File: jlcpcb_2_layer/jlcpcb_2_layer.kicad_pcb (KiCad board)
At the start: 2 copper layers, 2 parts

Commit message: updated JLCPCB 2layer template with new date
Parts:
- N2: value V20171120 -> V20180719
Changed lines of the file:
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@@
     (links 0)
     (no_connects 0)
-    (area 143.609505 97.866906 152.473829 108.0274)
+    (area 0 0 0 0)
     (thickness 1.6)
     (drawings 0)
@@
       (effects (font (size 1 1) (thickness 0.15)))
     )
-    (fp_text value V20171120 (at 0 0) (layer F.SilkS)
-      (effects (font (size 1 1) (thickness 0.15)))
-    )
+    (fp_text value V20180719 (at 0 0) (layer F.SilkS)
+      (effects (font (size 1 1) (thickness 0.15)))
+    )

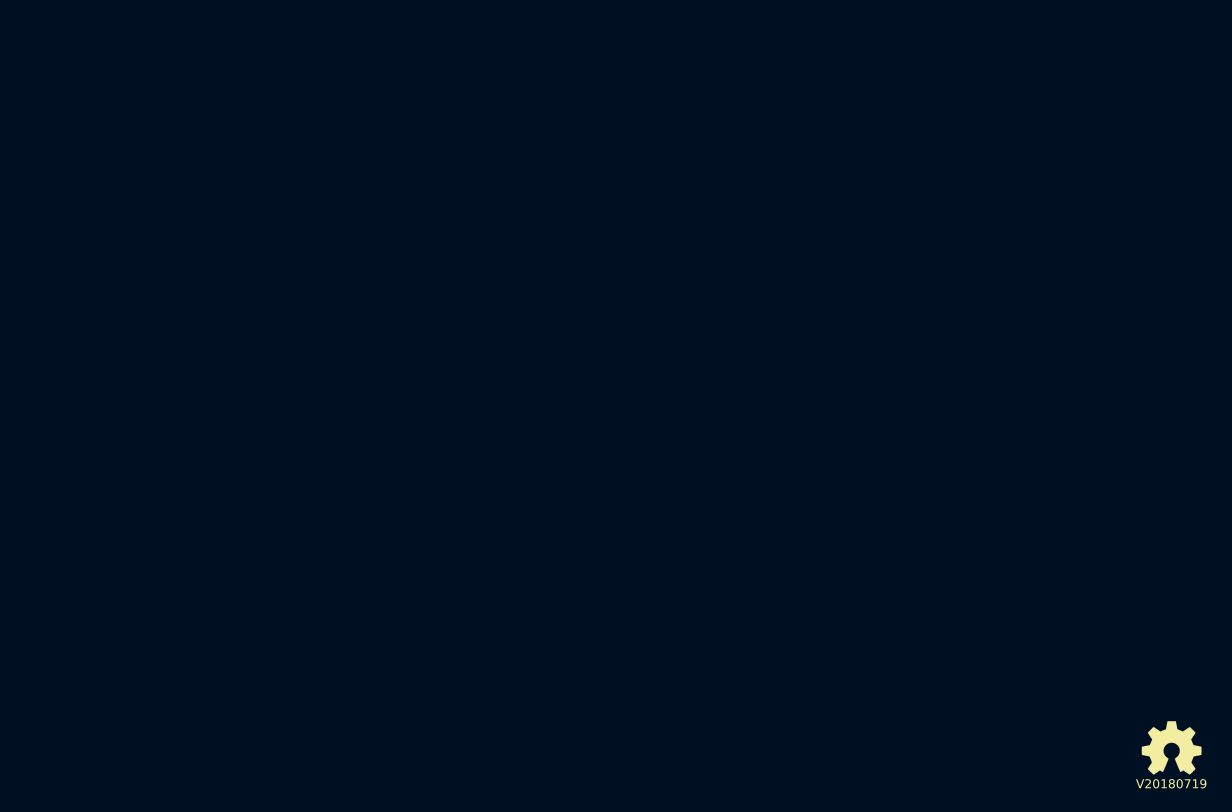
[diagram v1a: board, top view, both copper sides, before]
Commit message: updated jlcpcb 2 layer template to kicad 6
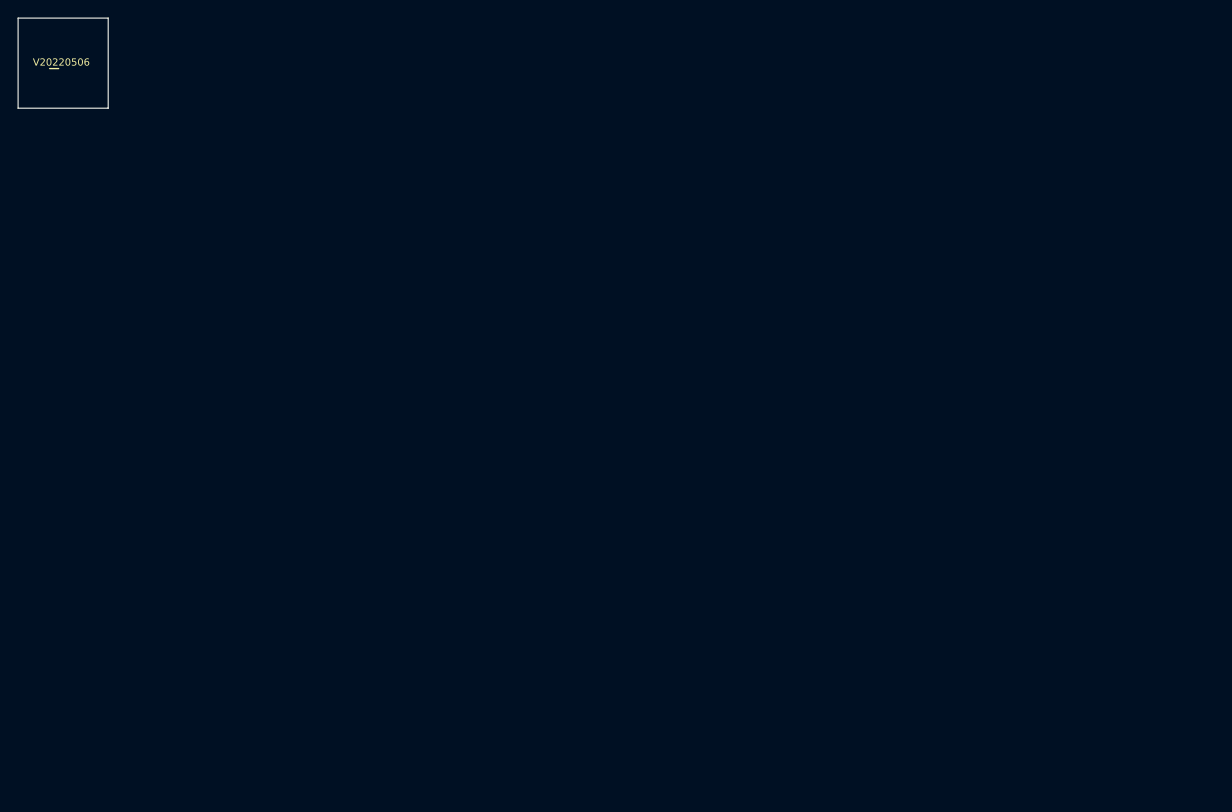
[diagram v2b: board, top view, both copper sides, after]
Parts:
- removed N2: V20180719, SquantorLabels:Label_version
- N1: value OHWLOGO -> V20220506; footprint Symbols:OSHW-Symbol_6.7x6mm_SilkScreen -> SquantorLabels:Label_Generic
- moved N1 145.4 mm to (24.0, 25.0)
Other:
- board outline added: 10 x 10 mm
- net class Default removed
- rule pad_to_mask_clearance: 0.2 -> 0.05
